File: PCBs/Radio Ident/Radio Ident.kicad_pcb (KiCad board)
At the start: 2 copper layers, 122.8 x 48.8 mm, 31 parts, among them SW1 SW_Push, SW2 SW_Push, SW3 SW_Push, SW4 SW_Push, SW5 SW_Push, SW6 SW_Push, U1 XIAO-ESP32-C3-SMD, U3 TYPE-C 6PLCH10.0 073

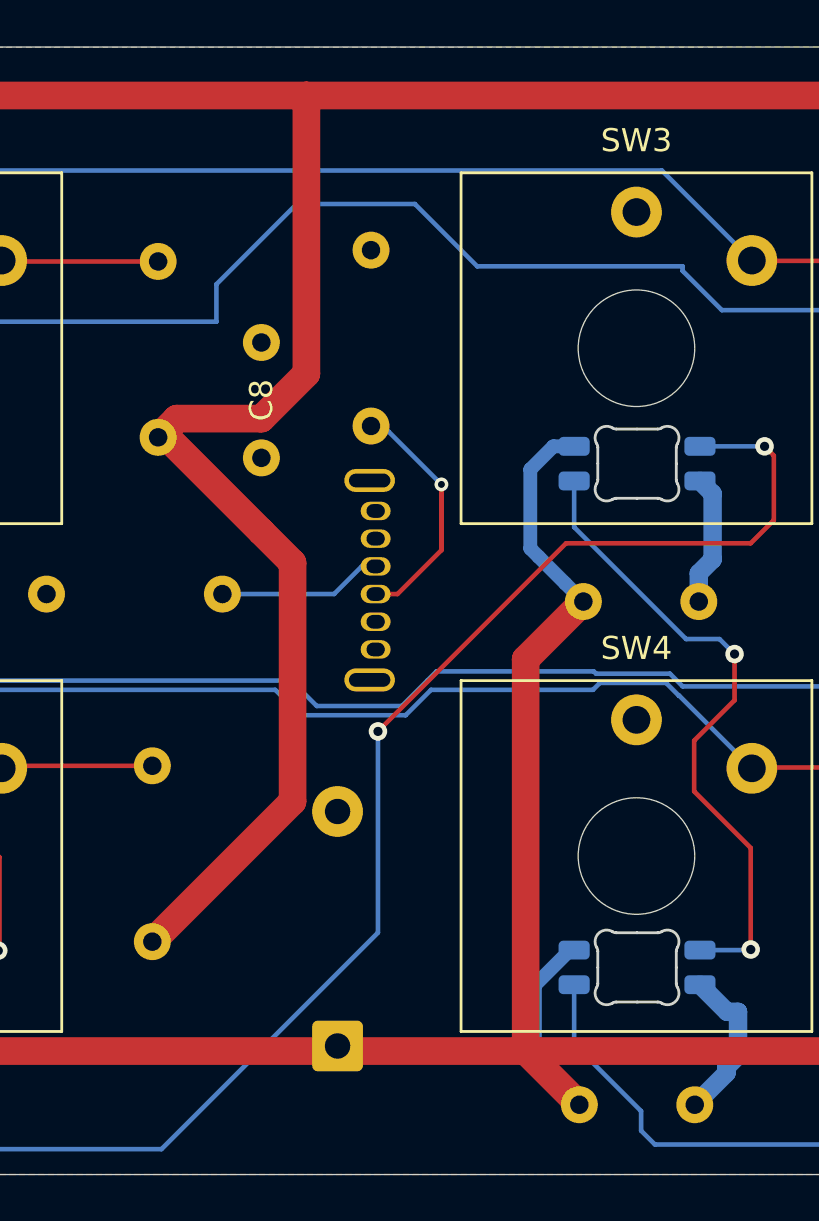
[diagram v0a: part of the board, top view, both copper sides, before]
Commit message: Update drill files and job configuration for radio panel PCBs
- Updated creation dates in NPTH and PTH drill files to 2026-08-13.
- Modified drill sizes for various tool definitions in NPTH and PTH files.
- Added new coordinates for tool paths in PTH drill file.
- Adjusted job configuration file creation date to 2026-08-13.
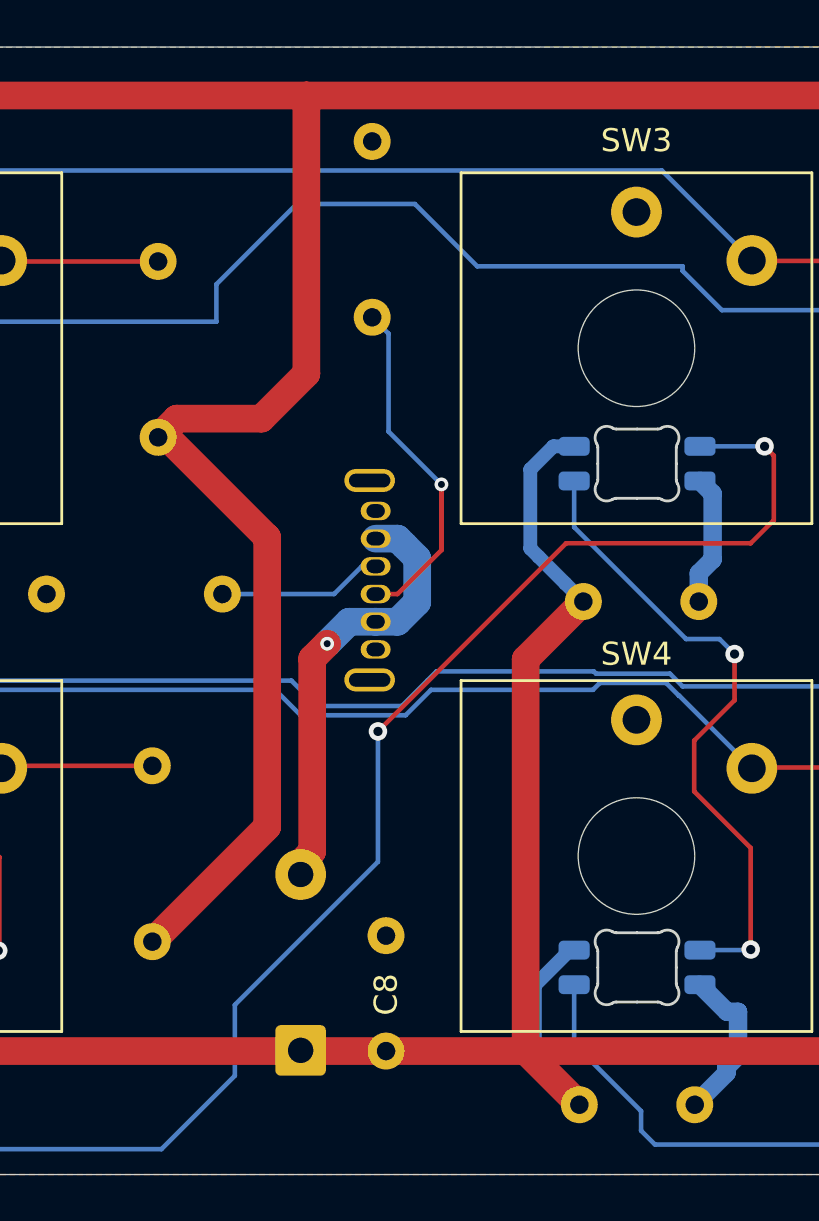
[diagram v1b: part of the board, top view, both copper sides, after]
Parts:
- D7: value D -> 1N5819; footprint Diode_THT:D_DO-41_SOD81_P10.16mm_Horizontal -> Diode_THT:D_DO-41_SOD81_P7.62mm_Horizontal
- moved C8 26.3 mm to (178.4, 111.0)
- moved R9 4.71 mm to (177.8, 79.2)
- moved D7 1.61 mm to (174.8, 111.0)
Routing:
- net Net-(D7-A): track 0.00 -> 19.2 mm, vias 0 -> 1
- net Net-(U3-CC2): track 13.6 -> 17.8 mm
- net +3.3V: track 265.7 -> 264.8 mm
